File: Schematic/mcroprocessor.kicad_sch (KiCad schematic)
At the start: 19 parts, among them J3 Conn_01x03_Pin, J3 DEBUG_HEADER, SW1 RESET, U1 STM32F091RCT6, U6 MAX7375AXR805

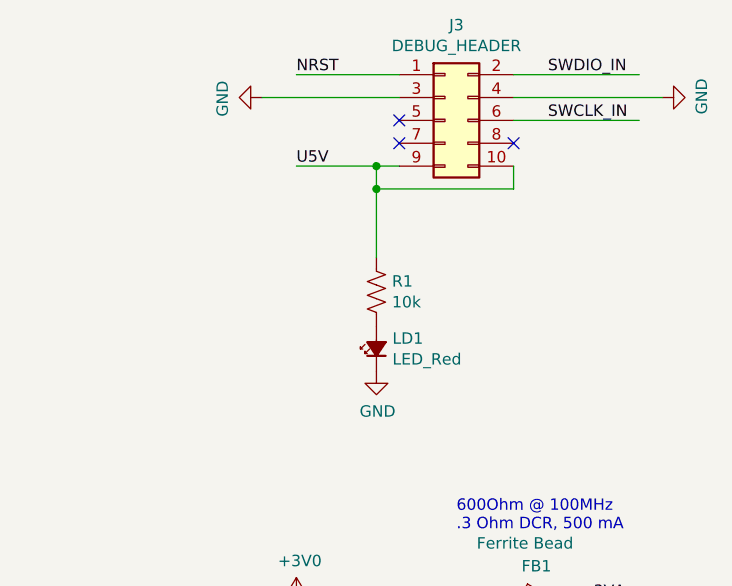
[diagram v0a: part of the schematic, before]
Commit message: Forgot to save the schematic from the last commit.
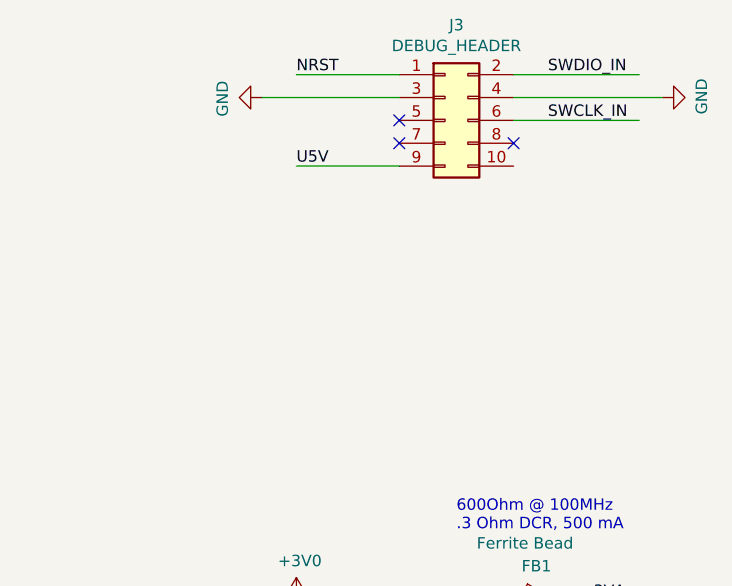
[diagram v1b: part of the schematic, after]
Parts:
- removed LD1: LED_Red, LED_THT:LED_D5.0mm, symbol stm32f091-rescue:LED_Small_ALT-Device
- removed R1: 10k, Resistor_SMD:R_1206_3216Metric_Pad1.30x1.75mm_HandSolder, symbol Device:R_US
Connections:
- net U5V: no longer J3.10 (Pin_10)

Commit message: Added level shifter (may or may not use) other minor fixes
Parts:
- removed J3: Conn_01x03_Pin, Connector_PinSocket_2.54mm:PinSocket_1x03_P2.54mm_Vertical, symbol Connector:Conn_01x03_Pin
- added J17: Conn_01x05_Pin, Connector_PinHeader_2.54mm:PinHeader_1x05_P2.54mm_Vertical, symbol Connector:Conn_01x05_Pin
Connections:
- net +3V0: now also J17.1 (Pin_1)
- net GND: now also J17.5 (Pin_5)
- net PA0: now also J17.2 (Pin_2)
- net PA1: now also J17.3 (Pin_3)
- net PA2: now also J17.4 (Pin_4)
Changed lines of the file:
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@@
     (stroke (width 0) (type default))
   )
-  (wire (pts (xy 106.68 133.35) (xy 114.3 133.35))
+  (wire (pts (xy 105.41 140.97) (xy 113.03 140.97))
     (stroke (width 0) (type default))
   )
@@
     (stroke (width 0) (type default))
   )
+  (wire (pts (xy 110.49 143.51) (xy 113.03 143.51))
+    (stroke (width 0) (type default))
+  )
   (wire (pts (xy 238.76 129.54) (xy 241.3 129.54))
     (stroke (width 0) (type default))
@@
     (stroke (width 0) (type default))
   )
-  (wire (pts (xy 106.68 130.81) (xy 114.3 130.81))
+  (wire (pts (xy 105.41 138.43) (xy 113.03 138.43))
     (stroke (width 0) (type default))
   )
@@
     (stroke (width 0) (type default))
   )
+  (wire (pts (xy 110.49 133.35) (xy 113.03 133.35))
+    (stroke (width 0) (type default))
+  )
   (wire (pts (xy 210.82 137.16) (xy 217.17 137.16))
     (stroke (width 0) (type default))
   )
-  (wire (pts (xy 106.68 128.27) (xy 114.3 128.27))
+  (wire (pts (xy 105.41 135.89) (xy 113.03 135.89))
     (stroke (width 0) (type default))
   )
@@
     )
   )
-  (global_label "PA0" (shape input) (at 106.68 128.27 180) (fields_autoplaced)
-    (effects (font (size 1.27 1.27)) (justify right))
-    (property "Intersheetrefs" "${INTERSHEET_REFS}" (at 100.2061 128.27 0)
+  (global_label "PA0" (shape input) (at 105.41 135.89 180) (fields_autoplaced)
+    (effects (font (size 1.27 1.27)) (justify right))
+    (property "Intersheetrefs" "${INTERSHEET_REFS}" (at 98.9361 135.89 0)
       (effects (font (size 1.27 1.27)) (justify right) hide)
     )
@@
     )
   )
-  (global_label "PA2" (shape input) (at 106.68 133.35 180) (fields_autoplaced)
-    (effects (font (size 1.27 1.27)) (justify right))
-    (property "Intersheetrefs" "${INTERSHEET_REFS}" (at 100.2061 133.35 0)
+  (global_label "PA2" (shape input) (at 105.41 140.97 180) (fields_autoplaced)
+    (effects (font (size 1.27 1.27)) (justify right))
+    (property "Intersheetrefs" "${INTERSHEET_REFS}" (at 98.9361 140.97 0)
       (effects (font (size 1.27 1.27)) (justify right) hide)
     )
@@
     )
   )
-  (global_label "PA1" (shape input) (at 106.68 130.81 180) (fields_autoplaced)
-    (effects (font (size 1.27 1.27)) (justify right))
-    (property "Intersheetrefs" "${INTERSHEET_REFS}" (at 100.2061 130.81 0)
+  (global_label "PA1" (shape input) (at 105.41 138.43 180) (fields_autoplaced)
+    (effects (font (size 1.27 1.27)) (justify right))
+    (property "Intersheetrefs" "${INTERSHEET_REFS}" (at 98.9361 138.43 0)
       (effects (font (size 1.27 1.27)) (justify right) hide)
     )
@@
     )
   )
+  (symbol (lib_id "Connector:Conn_01x05_Pin") (at 118.11 138.43 0) (mirror y) (unit 1)
+    (in_bom yes) (on_board yes) (dnp no) (fields_autoplaced)
+    (property "Reference" "J17" (at 118.8212 137.2179 0)
+      (effects (font (size 1.27 1.27)) (justify right))
+    )
+    (property "Value" "Conn_01x05_Pin" (at 118.8212 139.6421 0)
+      (effects (font (size 1.27 1.27)) (justify right))
+    )
+    (property "Footprint" "Connector_PinHeader_2.54mm:PinHeader_1x05_P2.54mm_Vertical" (at 118.11 138.43 0)
+      (effects (font (size 1.27 1.27)) hide)
+    )
+    (property "Datasheet" "~" (at 118.11 138.43 0)
+      (effects (font (size 1.27 1.27)) hide)
+    )
+    (pin "1")
+    (pin "2")
+    (pin "3")
+    (pin "4")
+    (pin "5")
+    (instances
+      (project "Schematic"
+        (path "/ced54cd9-3b34-40e4-aa66-964aaab81b0a/49528601-a054-44d2-8cd6-b055d7d9a1ef"
+          (reference "J17") (unit 1)
+        )
+      )
+    )
+  )
   (symbol (lib_id "power:+3V0") (at 154.94 77.47 270) (unit 1)
     (in_bom yes) (on_board yes) (dnp no)
@@
         (path "/ced54cd9-3b34-40e4-aa66-964aaab81b0a/575551e4-af3a-490e-80f8-c842b6f0dfe5"
           (reference "#PWR024") (unit 1)
-        )
-      )
-    )
-  )
-  (symbol (lib_id "Connector:Conn_01x03_Pin") (at 119.38 130.81 0) (mirror y) (unit 1)
-    (in_bom yes) (on_board yes) (dnp no)
-    (property "Reference" "J3" (at 114.3 121.92 0)
-      (effects (font (size 1.27 1.27)))
-    )
-    (property "Value" "Conn_01x03_Pin" (at 114.3 124.46 0)
-      (effects (font (size 1.27 1.27)))
-    )
-    (property "Footprint" "Connector_PinSocket_2.54mm:PinSocket_1x03_P2.54mm_Vertical" (at 119.38 130.81 0)
-      (effects (font (size 1.27 1.27)) hide)
-    )
-    (property "Datasheet" "~" (at 119.38 130.81 0)
-      (effects (font (size 1.27 1.27)) hide)
-    )
-    (pin "1")
-    (pin "2")
-    (pin "3")
-    (instances
-      (project "LM2678 - 5.0V"
-        (path "/519fb26c-708f-40e5-b123-022e0171115d"
-          (reference "J3") (unit 1)
-        )
-      )
-      (project "Schematic"
-        (path "/ced54cd9-3b34-40e4-aa66-964aaab81b0a/17b7dae5-2f82-4d17-9b49-7ea60414647f"
-          (reference "J6") (unit 1)
-        )
-        (path "/ced54cd9-3b34-40e4-aa66-964aaab81b0a/49528601-a054-44d2-8cd6-b055d7d9a1ef"
-          (reference "J17") (unit 1)
         )
       )
@@
         )
       )
+    )
+  )
+  (symbol (lib_id "power:GND") (at 110.49 143.51 0) (unit 1)
+    (in_bom yes) (on_board yes) (dnp no)
+    (property "Reference" "#PWR0130" (at 110.49 149.86 0)
+      (effects (font (size 1.27 1.27)) hide)
+    )
+    (property "Value" "GND" (at 110.617 147.9042 0)
+      (effects (font (size 1.27 1.27)))
+    )
+    (property "Footprint" "" (at 110.49 143.51 0)
+      (effects (font (size 1.27 1.27)) hide)
+    )
+    (property "Datasheet" "" (at 110.49 143.51 0)
+      (effects (font (size 1.27 1.27)) hide)
+    )
+    (pin "1")
+    (instances
+      (project "stm32f091"
+        (path "/1a854c3f-f20e-4271-9c06-678b7140bb2e"
+          (reference "#PWR0130") (unit 1)
+        )
+      )
+      (project "Schematic"
+        (path "/ced54cd9-3b34-40e4-aa66-964aaab81b0a/49528601-a054-44d2-8cd6-b055d7d9a1ef"
+          (reference "#PWR089") (unit 1)
+        )
+        (path "/ced54cd9-3b34-40e4-aa66-964aaab81b0a"
+          (reference "#PWR019") (unit 1)
+        )
+        (path "/ced54cd9-3b34-40e4-aa66-964aaab81b0a/1629468b-8e9d-4ab7-97ca-858e6989be67"
+          (reference "#PWR024") (unit 1)
+        )
+        (path "/ced54cd9-3b34-40e4-aa66-964aaab81b0a/575551e4-af3a-490e-80f8-c842b6f0dfe5"
+          (reference "#PWR024") (unit 1)
+        )
+      )
+    )
+  )
+  (symbol (lib_id "power:+3V0") (at 110.49 133.35 0) (unit 1)
+    (in_bom yes) (on_board yes) (dnp no)
+    (property "Reference" "#PWR0104" (at 110.49 137.16 0)
+      (effects (font (size 1.27 1.27)) hide)
+    )
+    (property "Value" "+3V0" (at 110.871 128.9558 0)
+      (effects (font (size 1.27 1.27)))
+    )
+    (property "Footprint" "" (at 110.49 133.35 0)
+      (effects (font (size 1.27 1.27)) hide)
+    )
+    (property "Datasheet" "" (at 110.49 133.35 0)
+      (effects (font (size 1.27 1.27)) hide)
+    )
+    (pin "1")
+    (instances
+      (project "stm32f091"
+        (path "/1a854c3f-f20e-4271-9c06-678b7140bb2e"
+          (reference "#PWR0104") (unit 1)
+        )
+      )
+      (project "Schematic"
+        (path "/ced54cd9-3b34-40e4-aa66-964aaab81b0a/49528601-a054-44d2-8cd6-b055d7d9a1ef"
+          (reference "#PWR088") (unit 1)
+        )
+      )

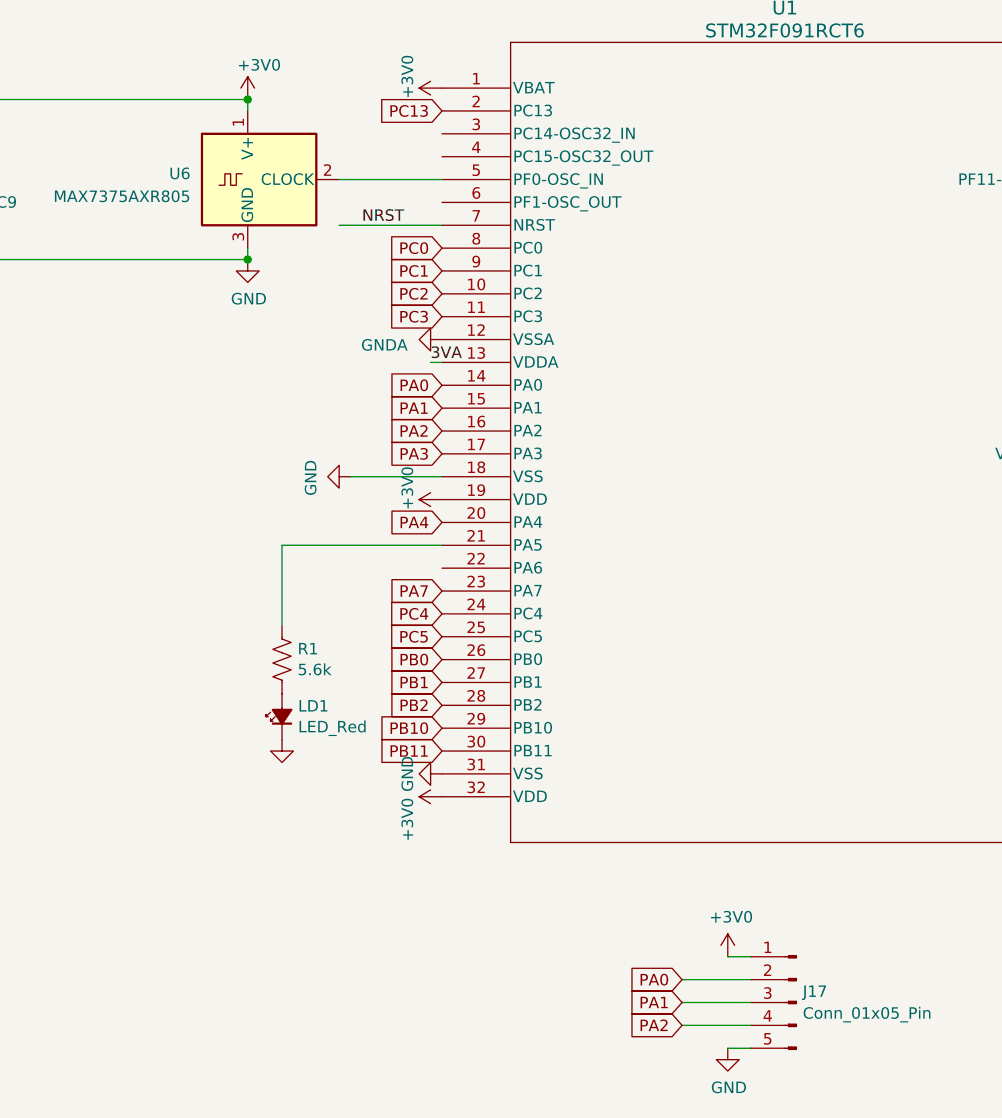
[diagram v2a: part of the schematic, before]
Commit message: relabeld all of the components so they have more resonable numbers
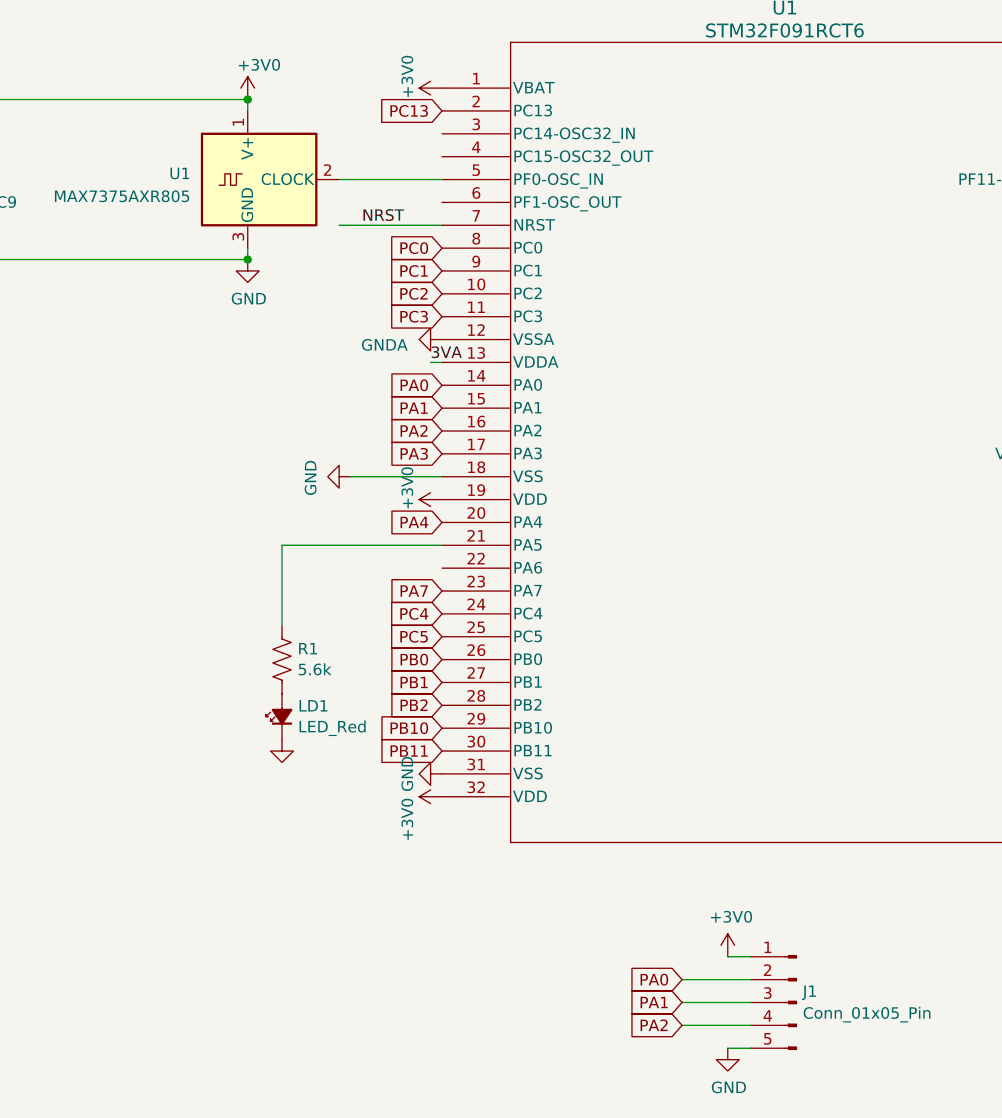
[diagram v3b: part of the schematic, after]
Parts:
- renumbered J17 to J1, U6 to U1
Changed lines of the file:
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@@
         )
         (path "/ced54cd9-3b34-40e4-aa66-964aaab81b0a/49528601-a054-44d2-8cd6-b055d7d9a1ef"
-          (reference "#PWR010") (unit 1)
+          (reference "#PWR06") (unit 1)
         )
       )
@@
       (project "Schematic"
         (path "/ced54cd9-3b34-40e4-aa66-964aaab81b0a/49528601-a054-44d2-8cd6-b055d7d9a1ef"
-          (reference "C5") (unit 1)
+          (reference "C6") (unit 1)
         )
       )
@@
         )
         (path "/ced54cd9-3b34-40e4-aa66-964aaab81b0a/49528601-a054-44d2-8cd6-b055d7d9a1ef"
-          (reference "#PWR031") (unit 1)
+          (reference "#PWR023") (unit 1)
         )
       )
@@
   (symbol (lib_id "Oscillator:MAX7375AXR805") (at 57.15 46.99 0) (unit 1)
     (in_bom yes) (on_board yes) (dnp no) (fields_autoplaced)
-    (property "Reference" "U6" (at 50.8 46.355 0)
+    (property "Reference" "U1" (at 50.8 46.355 0)
       (effects (font (size 1.27 1.27)) (justify right))
     )
@@
       (project "Schematic"
         (path "/ced54cd9-3b34-40e4-aa66-964aaab81b0a/49528601-a054-44d2-8cd6-b055d7d9a1ef"
-          (reference "U6") (unit 1)
+          (reference "U1") (unit 1)
         )
       )
@@
   (symbol (lib_id "Connector:Conn_01x05_Pin") (at 118.11 138.43 0) (mirror y) (unit 1)
     (in_bom yes) (on_board yes) (dnp no) (fields_autoplaced)
-    (property "Reference" "J17" (at 118.8212 137.2179 0)
+    (property "Reference" "J1" (at 118.8212 137.2179 0)
       (effects (font (size 1.27 1.27)) (justify right))
     )
@@
       (project "Schematic"
         (path "/ced54cd9-3b34-40e4-aa66-964aaab81b0a/49528601-a054-44d2-8cd6-b055d7d9a1ef"
-          (reference "J17") (unit 1)
+          (reference "J1") (unit 1)
         )
       )
@@
       (project "Schematic"
         (path "/ced54cd9-3b34-40e4-aa66-964aaab81b0a/49528601-a054-44d2-8cd6-b055d7d9a1ef"
-          (reference "#PWR03") (unit 1)
+          (reference "#PWR014") (unit 1)
         )
       )
@@
       (project "Schematic"
         (path "/ced54cd9-3b34-40e4-aa66-964aaab81b0a/49528601-a054-44d2-8cd6-b055d7d9a1ef"
-          (reference "#PWR015") (unit 1)
+          (reference "#PWR021") (unit 1)
         )
         (path "/ced54cd9-3b34-40e4-aa66-964aaab81b0a"
@@
       (project "Schematic"
         (path "/ced54cd9-3b34-40e4-aa66-964aaab81b0a/49528601-a054-44d2-8cd6-b055d7d9a1ef"
-          (reference "#PWR07") (unit 1)
+          (reference "#PWR022") (unit 1)
         )
         (path "/ced54cd9-3b34-40e4-aa66-964aaab81b0a"
@@
       (project "Schematic"
         (path "/ced54cd9-3b34-40e4-aa66-964aaab81b0a/49528601-a054-44d2-8cd6-b055d7d9a1ef"
-          (reference "#PWR014") (unit 1)
+          (reference "#PWR020") (unit 1)
         )
       )
@@
       (project "Schematic"
         (path "/ced54cd9-3b34-40e4-aa66-964aaab81b0a/49528601-a054-44d2-8cd6-b055d7d9a1ef"
-          (reference "#PWR036") (unit 1)
+          (reference "#PWR024") (unit 1)
         )
         (path "/ced54cd9-3b34-40e4-aa66-964aaab81b0a"
@@
       (project "Schematic"
         (path "/ced54cd9-3b34-40e4-aa66-964aaab81b0a/49528601-a054-44d2-8cd6-b055d7d9a1ef"
-          (reference "C1") (unit 1)
+          (reference "C5") (unit 1)
         )
       )
@@
       (project "Schematic"
         (path "/ced54cd9-3b34-40e4-aa66-964aaab81b0a/49528601-a054-44d2-8cd6-b055d7d9a1ef"
-          (reference "#PWR016") (unit 1)
+          (reference "#PWR019") (unit 1)
         )
         (path "/ced54cd9-3b34-40e4-aa66-964aaab81b0a"
@@
       (project "Schematic"
         (path "/ced54cd9-3b34-40e4-aa66-964aaab81b0a/49528601-a054-44d2-8cd6-b055d7d9a1ef"
-          (reference "R44") (unit 1)
+          (reference "R1") (unit 1)
         )
       )
@@
       (project "Schematic"
         (path "/ced54cd9-3b34-40e4-aa66-964aaab81b0a/49528601-a054-44d2-8cd6-b055d7d9a1ef"
-          (reference "#PWR047") (unit 1)
+          (reference "#PWR02") (unit 1)
         )
         (path "/ced54cd9-3b34-40e4-aa66-964aaab81b0a"
@@
       (project "Schematic"
         (path "/ced54cd9-3b34-40e4-aa66-964aaab81b0a/49528601-a054-44d2-8cd6-b055d7d9a1ef"
-          (reference "LD6") (unit 1)
+          (reference "LD1") (unit 1)
         )
       )
@@
       (project "Schematic"
         (path "/ced54cd9-3b34-40e4-aa66-964aaab81b0a/49528601-a054-44d2-8cd6-b055d7d9a1ef"
-          (reference "C6") (unit 1)
+          (reference "C7") (unit 1)
         )
       )
@@
       (project "Schematic"
         (path "/ced54cd9-3b34-40e4-aa66-964aaab81b0a/49528601-a054-44d2-8cd6-b055d7d9a1ef"
-          (reference "#PWR04") (unit 1)
+          (reference "#PWR012") (unit 1)
         )
       )
@@
       (project "Schematic"
         (path "/ced54cd9-3b34-40e4-aa66-964aaab81b0a/49528601-a054-44d2-8cd6-b055d7d9a1ef"
-          (reference "#PWR011") (unit 1)
+          (reference "#PWR013") (unit 1)
         )
         (path "/ced54cd9-3b34-40e4-aa66-964aaab81b0a"
@@
       (project "Schematic"
         (path "/ced54cd9-3b34-40e4-aa66-964aaab81b0a/49528601-a054-44d2-8cd6-b055d7d9a1ef"
-          (reference "J5") (unit 1)
+          (reference "J2") (unit 1)
         )
       )
@@
       (project "Schematic"
         (path "/ced54cd9-3b34-40e4-aa66-964aaab81b0a/49528601-a054-44d2-8cd6-b055d7d9a1ef"
-          (reference "#PWR06") (unit 1)
+          (reference "#PWR017") (unit 1)
         )
       )
@@
       (project "Schematic"
         (path "/ced54cd9-3b34-40e4-aa66-964aaab81b0a/49528601-a054-44d2-8cd6-b055d7d9a1ef"
-          (reference "#PWR02") (unit 1)
+          (reference "#PWR07") (unit 1)
         )
       )
@@
       (project "Schematic"
         (path "/ced54cd9-3b34-40e4-aa66-964aaab81b0a/49528601-a054-44d2-8cd6-b055d7d9a1ef"
-          (reference "#PWR089") (unit 1)
+          (reference "#PWR011") (unit 1)
         )
         (path "/ced54cd9-3b34-40e4-aa66-964aaab81b0a"
@@
       (project "Schematic"
         (path "/ced54cd9-3b34-40e4-aa66-964aaab81b0a/49528601-a054-44d2-8cd6-b055d7d9a1ef"
-          (reference "#PWR088") (unit 1)
+          (reference "#PWR010") (unit 1)
         )
       )
@@
       (project "Schematic"
         (path "/ced54cd9-3b34-40e4-aa66-964aaab81b0a/49528601-a054-44d2-8cd6-b055d7d9a1ef"
-          (reference "C16") (unit 1)
+          (reference "C1") (unit 1)
         )
       )
@@
       (project "Schematic"
         (path "/ced54cd9-3b34-40e4-aa66-964aaab81b0a/49528601-a054-44d2-8cd6-b055d7d9a1ef"
-          (reference "#PWR01") (unit 1)
+          (reference "#PWR09") (unit 1)
         )
       )
@@
       (project "Schematic"
         (path "/ced54cd9-3b34-40e4-aa66-964aaab81b0a/49528601-a054-44d2-8cd6-b055d7d9a1ef"
-          (reference "#PWR033") (unit 1)
+          (reference "#PWR016") (unit 1)
         )
         (path "/ced54cd9-3b34-40e4-aa66-964aaab81b0a"
@@
       (project "Schematic"
         (path "/ced54cd9-3b34-40e4-aa66-964aaab81b0a/49528601-a054-44d2-8cd6-b055d7d9a1ef"
-          (reference "#PWR041") (unit 1)
+          (reference "#PWR01") (unit 1)
         )
       )
@@
       (project "Schematic"
         (path "/ced54cd9-3b34-40e4-aa66-964aaab81b0a/49528601-a054-44d2-8cd6-b055d7d9a1ef"
-          (reference "#PWR012") (unit 1)
+          (reference "#PWR015") (unit 1)
         )
         (path "/ced54cd9-3b34-40e4-aa66-964aaab81b0a"
@@
       (project "Schematic"
         (path "/ced54cd9-3b34-40e4-aa66-964aaab81b0a/49528601-a054-44d2-8cd6-b055d7d9a1ef"
-          (reference "#PWR048") (unit 1)
+          (reference "#PWR03") (unit 1)
         )
       )
@@
       (project "Schematic"
         (path "/ced54cd9-3b34-40e4-aa66-964aaab81b0a/49528601-a054-44d2-8cd6-b055d7d9a1ef"
-          (reference "#PWR09") (unit 1)
+          (reference "#PWR04") (unit 1)
         )
         (path "/ced54cd9-3b34-40e4-aa66-964aaab81b0a"
@@
       (project "Schematic"
         (path "/ced54cd9-3b34-40e4-aa66-964aaab81b0a/49528601-a054-44d2-8cd6-b055d7d9a1ef"
-          (reference "#PWR013") (unit 1)
+          (reference "#PWR018") (unit 1)
         )
       )
@@
       (project "Schematic"
         (path "/ced54cd9-3b34-40e4-aa66-964aaab81b0a/49528601-a054-44d2-8cd6-b055d7d9a1ef"
-          (reference "R1") (unit 1)
-        )
-      )
+          (reference "R3") (unit 1)
+        )
+      )
